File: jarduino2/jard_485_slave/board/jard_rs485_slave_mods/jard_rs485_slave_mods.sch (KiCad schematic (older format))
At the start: 25 parts, among them J1 NETWORK IN, J2 NETWORK OUT, J3 LED, J4 LED, J5 Debit, J6 Niveau, J7 Electrovanne 12V, Q1 BPC_2N2222A, Q2 P03P4L-04, U1 BPC_Mod485, U2 BPC_DHT22

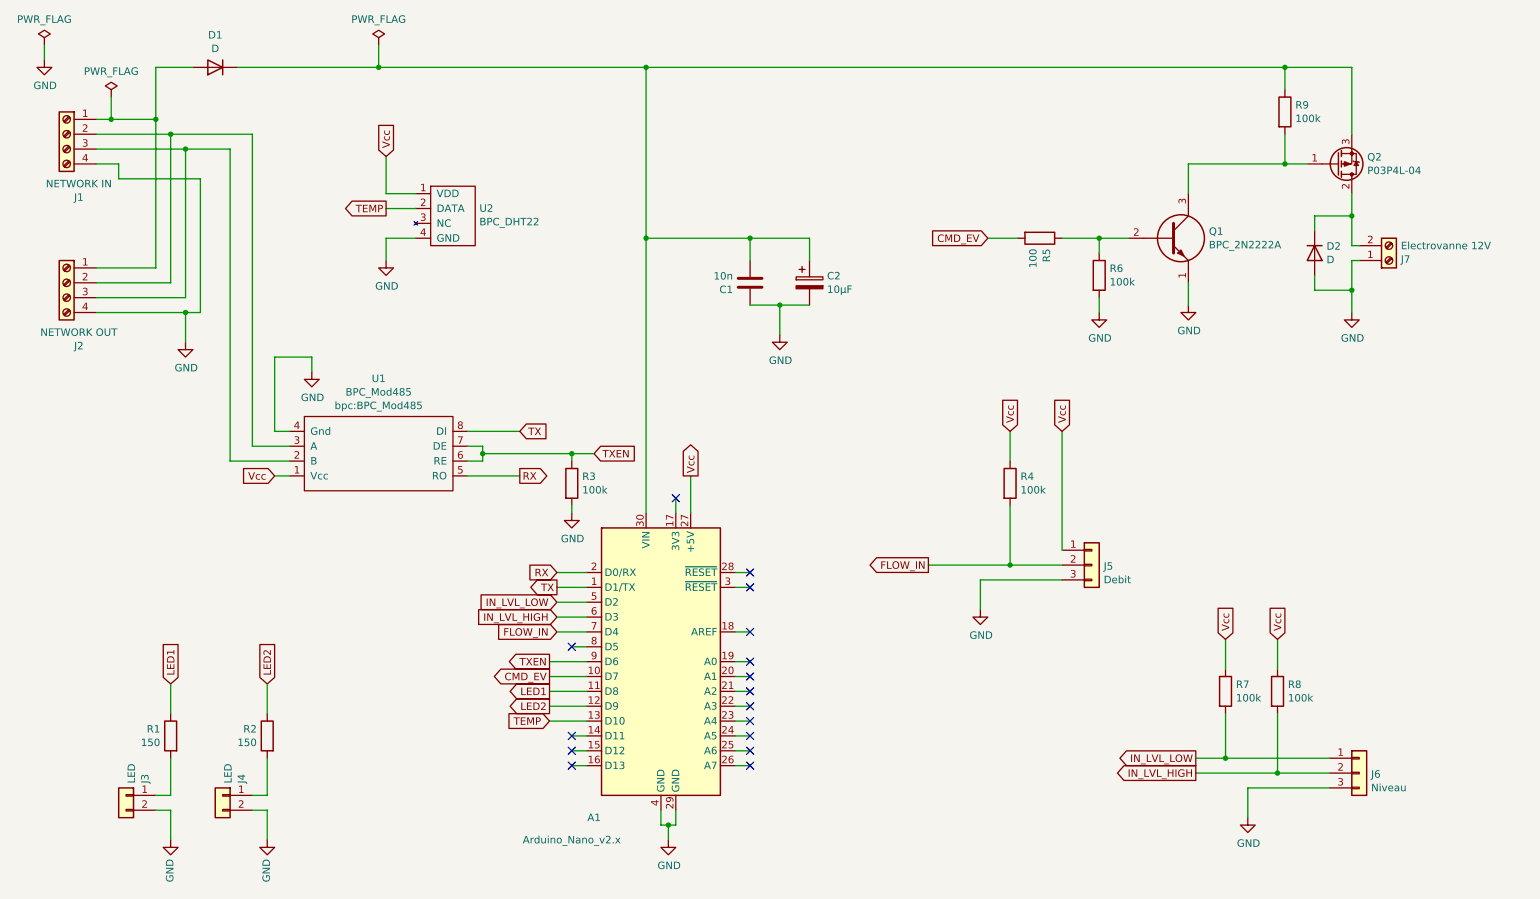
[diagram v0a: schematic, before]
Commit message: Ajout AO de mesure de courant + mesure de tension
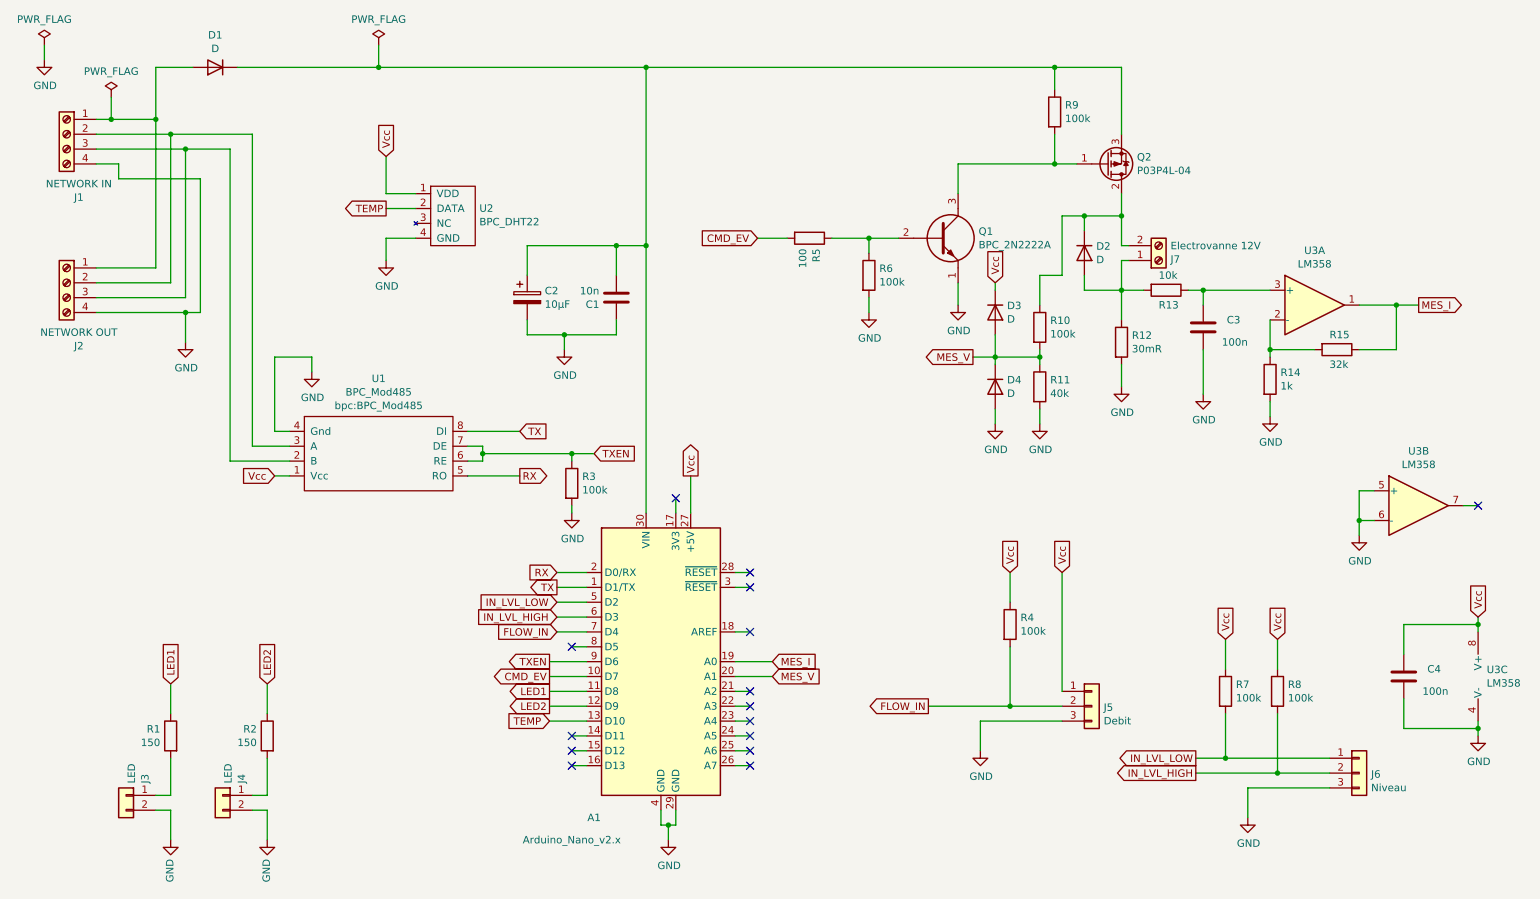
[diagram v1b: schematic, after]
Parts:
- added C3, C4: 100n, Capacitor_THT:C_Disc_D5.0mm_W2.5mm_P2.50mm, symbol Device:C
- added D3, D4: D, Diode_THT:D_A-405_P2.54mm_Vertical_AnodeUp, symbol Device:D
- added R10: 100k, Resistor_THT:R_Axial_DIN0309_L9.0mm_D3.2mm_P2.54mm_Vertical, symbol Device:R
- added R11: 40k, Resistor_THT:R_Axial_DIN0309_L9.0mm_D3.2mm_P2.54mm_Vertical, symbol Device:R
- added R12: 30mR, Resistor_THT:R_Axial_DIN0309_L9.0mm_D3.2mm_P2.54mm_Vertical, symbol Device:R
- added R13: 10k, Resistor_THT:R_Axial_DIN0309_L9.0mm_D3.2mm_P2.54mm_Vertical, symbol Device:R
- added R14: 1k, Resistor_THT:R_Axial_DIN0309_L9.0mm_D3.2mm_P2.54mm_Vertical, symbol Device:R
- added R15: 32k, Resistor_THT:R_Axial_DIN0309_L9.0mm_D3.2mm_P2.54mm_Vertical, symbol Device:R
- added U3: LM358, Package_DIP:DIP-8_W7.62mm_Socket_LongPads, symbol Amplifier_Operational:LM358
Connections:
- net GND: now also C3.1, C4.1, D4.2 (A), R11.2, R12.2, R14.2, U3.4 (V-), U3.5 (+), U3.6 (-); no longer D2.2 (A), J7.1 (Pin_1)
- net Vcc: now also C4.2, D3.1 (K), U3.8 (V+)
- net at D2.1 (K), J7.2 (Pin_2), Q2.2 (D): now also R10.1
- net MES_I: now reaches A1.19 (A0)
- net MES_I: now also R15.1, U3.1
- net MES_V: now reaches A1.20 (A1)
- net MES_V: now also D3.2 (A), D4.1 (K), R10.2, R11.1
- new net: D2.2 (A), J7.1 (Pin_1), R12.1, R13.2
- new net: R14.1, R15.2, U3.2 (-)
- new net: C3.2, R13.1, U3.3 (+)
- no-connect marks 16 -> 15
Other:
- moved on the sheet: C1, C2, D2, J5, J7, Q1, Q2, R4, R5, R6, R9

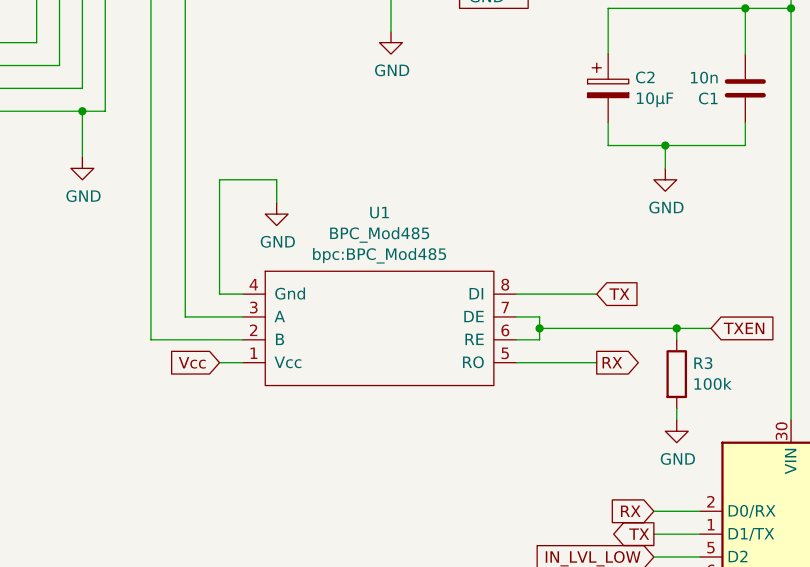
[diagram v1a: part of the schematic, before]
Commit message: Correction inversion RX/TX
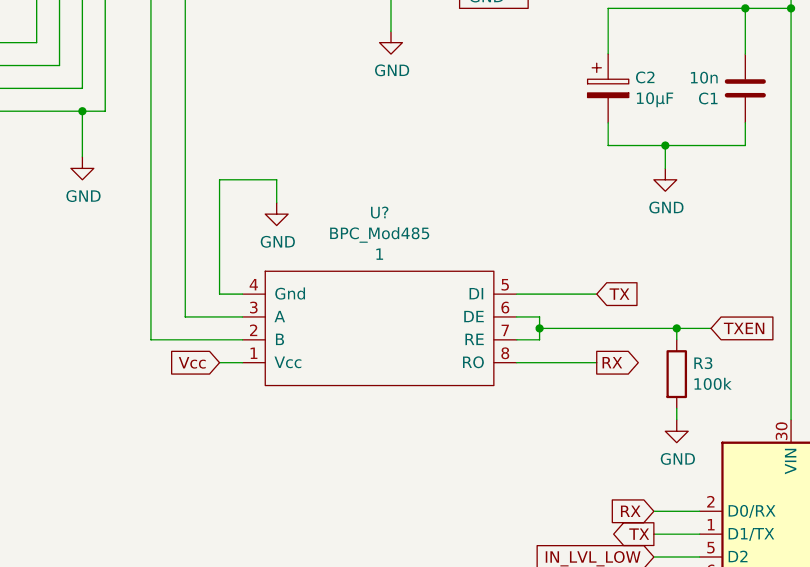
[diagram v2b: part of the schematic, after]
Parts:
- removed U1: BPC_Mod485, bpc:BPC_Mod485, symbol bpc_scm:BPC_Mod485
- added U?: BPC_Mod485, bpc:BPC_Mod485, symbol bpc:BPC_Mod485
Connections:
- net GND: now also U?.4 (Gnd)
- net RX: now also U?.8 (RO)
- net TX: now also U?.5 (DI)
- net TXEN: now also U?.6 (DE), U?.7 (RE)
- net Vcc: now also U?.1 (Vcc)
- net at J1.2 (Pin_2), J2.2 (Pin_2): now also U?.3 (A)
- net at J1.3 (Pin_3), J2.3 (Pin_3): now also U?.2 (B)
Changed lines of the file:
@@
 	1600 950  1600 1300
 Connection ~ 1600 1300
-$Comp
-L bpc_scm:BPC_Mod485 U1
-U 1 1 63E332DA
-P 2600 3700
-F 0 "U1" H 3100 4355 50  0000 C CNN
-F 1 "BPC_Mod485" H 3100 4264 50  0000 C CNN
-F 2 "bpc:BPC_Mod485" H 3100 4173 50  0000 C CNN
-F 3 "" H 3000 3700 50  0001 C CNN
-	1    2600 3700
-	1    0    0    -1
-$EndComp
 Wire Wire Line
 	2500 3600 2100 3600
@@
 Wire Wire Line
 	10500 5400 10500 5350
+$Comp
+L bpc:BPC_Mod485 U?
+U 1 1 645989A1
+P 2600 3700
+F 0 "U?" H 3100 4355 50  0000 C CNN
+F 1 "BPC_Mod485" H 3100 4264 50  0000 C CNN
+F 2 "bpc:BPC_Mod485" H 3000 3700 50  0001 C CNN
+F 3 "" H 3000 3700 50  0001 C CNN
+F 4 "1" H 3100 4173 50  0000 C CNN "Bpcref"
+	1    2600 3700
+	1    0    0    -1
+$EndComp
 $EndSCHEMATC

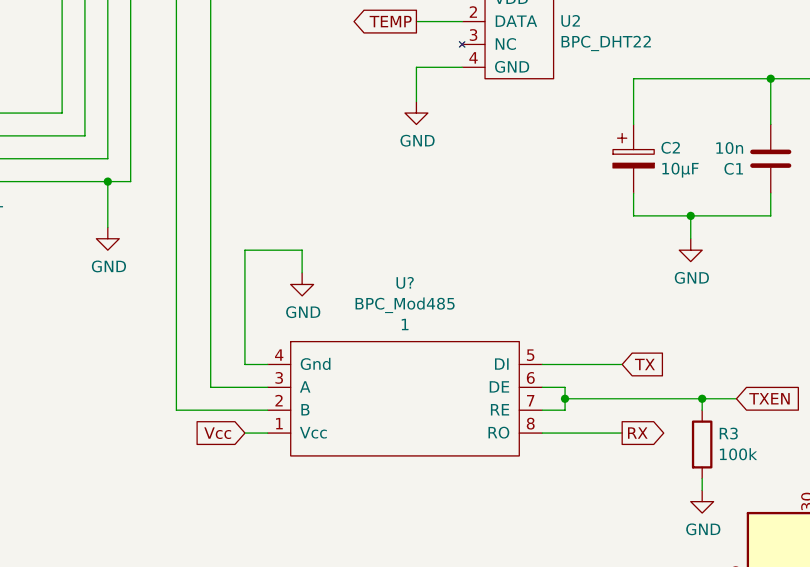
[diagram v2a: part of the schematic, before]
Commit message: Agrandir sérigraphie connecteurs bus Correction erreur inversion sérigraphie 1 et 4 sur J2 Correction inversion RX/TX sur module RS485 Inversion sérigraphie Niveaux/Débit
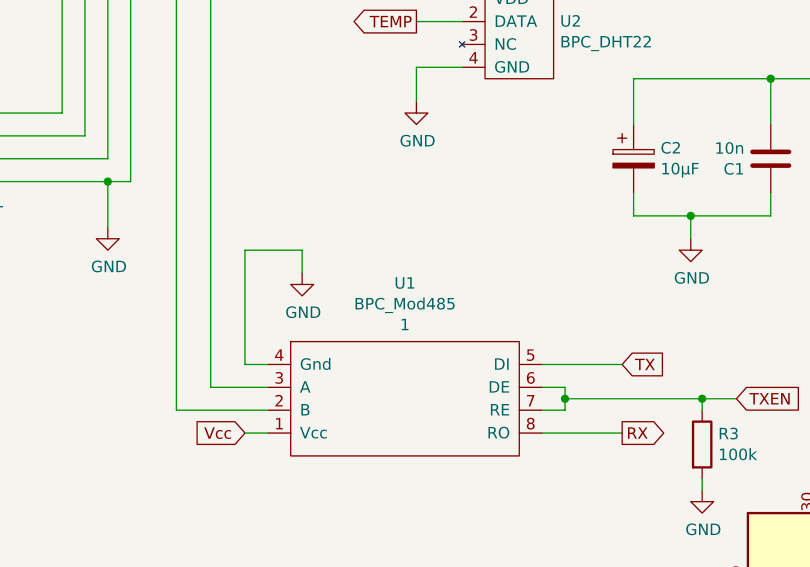
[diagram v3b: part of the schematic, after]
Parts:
- gave numbers to parts that had none: 1
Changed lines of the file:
@@
 Sheet 1 1
 Title "Carte de commande d'un Oya par RS485"
-Date "2023-03-06"
-Rev "A0"
+Date "2023-05-08"
+Rev "B0"
 Comp "BPC"
 Comment1 ""
@@
 	10500 5400 10500 5350
 $Comp
-L bpc:BPC_Mod485 U?
+L bpc:BPC_Mod485 U1
 U 1 1 645989A1
 P 2600 3700
-F 0 "U?" H 3100 4355 50  0000 C CNN
+F 0 "U1" H 3100 4355 50  0000 C CNN
 F 1 "BPC_Mod485" H 3100 4264 50  0000 C CNN
 F 2 "bpc:BPC_Mod485" H 3000 3700 50  0001 C CNN
